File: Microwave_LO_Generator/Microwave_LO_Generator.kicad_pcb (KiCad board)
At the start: 4 copper layers, 49.5 x 47 mm, 59 parts, among them IC1 ADP150AUJZ-3.3-R7, J4 Conn_01x05_Male, U1 ADF4150HV, U2 LM317L_SO8, U3 LM317L_SO8, U4 HMC739LP4E, X1 IQXT-220-1

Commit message: update
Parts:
- added J5: Conn_01x01_Female, Microwave_LO_Generator:Connettore, F.Cu at (141.8, 99.9)
- moved C1 135.1 mm to (95.6, 95.1)
- moved C10 135.1 mm to (110.2, 102.8)
- moved C12 135.1 mm to (110.2, 104.0)
- moved C13 135.1 mm to (114.9, 103.8)
- moved C15 135.1 mm to (122.9, 103.9)
- moved C18 135.1 mm to (100.1, 109.7)
- moved C2 135.1 mm to (95.6, 93.9)
- moved C20 135.1 mm to (109.6, 118.6)
- moved C23 135.1 mm to (100.1, 84.3)
- moved C24 135.1 mm to (100.1, 86.2)
- moved C26 135.1 mm to (130.6, 102.8)
- moved C28 135.1 mm to (117.6, 98.2)
- moved C30 135.1 mm to (135.0, 94.5)
- moved C4 135.1 mm to (103.9, 97.0)
- moved C6 135.1 mm to (113.7, 94.5)
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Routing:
- net Net-(J5-Pad1): track 0.00 -> 5.42 mm
- net 0: vias 27 -> 29
- net (no net): vias 0 -> 6
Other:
- board size 49.5 x 47 mm -> 53.3 x 45.7 mm

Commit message: Power Supply update
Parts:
- removed C18, C20: 1u, Capacitor_SMD:C_0402_1005Metric_Pad0.74x0.62mm_HandSolder
- removed D3, D4, D5, D6: DIODE, Diode_SMD:D_MELF
- removed IC1: ADP150AUJZ-3.3-R7, SamacSys_Parts:SOT95P280X100-5N
- removed R10: 720r, Resistor_SMD:R_0402_1005Metric_Pad0.72x0.64mm_HandSolder
- removed R7: 0r, Resistor_SMD:R_0402_1005Metric_Pad0.72x0.64mm_HandSolder
- removed R9: 240r, Resistor_SMD:R_0402_1005Metric_Pad0.72x0.64mm_HandSolder
- added C3: 100p, Capacitor_SMD:C_0402_1005Metric_Pad0.74x0.62mm_HandSolder, F.Cu at (103.2, 109.4)
- added C31: 100p, Capacitor_SMD:C_0402_1005Metric_Pad0.74x0.62mm_HandSolder, F.Cu at (129.3, 110.7)
- added C32: 10n, Capacitor_SMD:C_0402_1005Metric_Pad0.74x0.62mm_HandSolder, F.Cu at (116.6, 84.0)
- added C33: 10n, Capacitor_SMD:C_0402_1005Metric_Pad0.74x0.62mm_HandSolder, F.Cu at (137.5, 90.3)
- added C34: 10n, Capacitor_SMD:C_0402_1005Metric_Pad0.74x0.62mm_HandSolder, F.Cu at (124.2, 107.5)
- added C35: 3.3u, Capacitor_SMD:C_0402_1005Metric_Pad0.74x0.62mm_HandSolder, F.Cu at (131.8, 94.1)
- added C36: 3.3u, Capacitor_SMD:C_0402_1005Metric_Pad0.74x0.62mm_HandSolder, F.Cu at (124.2, 104.9)
- added C5: 100p, Capacitor_SMD:C_0402_1005Metric_Pad0.74x0.62mm_HandSolder, F.Cu at (108.3, 111.9)
- added J1: Conn_01x02_Male, Connector_PinHeader_2.54mm:PinHeader_1x02_P2.54mm_Vertical, F.Cu at (102.0, 117.0)
- added J2: Conn_01x02_Male, Connector_PinHeader_2.54mm:PinHeader_1x02_P2.54mm_Vertical, F.Cu at (96.9, 86.5)
- added TP1: TestPoint, TestPoint:TestPoint_Loop_D2.60mm_Drill1.6mm_Beaded, F.Cu at (83.2, 92.5)
- added TP2: TestPoint, TestPoint:TestPoint_Loop_D2.60mm_Drill1.6mm_Beaded, F.Cu at (78.1, 92.5)
- added U5: LT1962-5, Package_SO:MSOP-8_3x3mm_P0.65mm, F.Cu at (133.1, 91.6)
- added U6: LT1962-5, Package_SO:MSOP-8_3x3mm_P0.65mm, F.Cu at (128.0, 107.5)
- C17, C19: value 1u -> 4.7u
- C21: value 1u -> 100p
- C25: value 1u -> 3.3u
- R11: value 240r -> 1K8
- R12: value 1K488 -> 300r
- R8: value 0r -> 10r
- U2: value LM317L_SO8 -> LT1962-3.3; footprint Package_SO:SOIC-8_3.9x4.9mm_P1.27mm -> Package_SO:MSOP-8_3x3mm_P0.65mm
- U3: value LM317L_SO8 -> LT3010; footprint Package_SO:SOIC-8_3.9x4.9mm_P1.27mm -> Package_SO:MSOP-8-1EP_3x3mm_P0.65mm_EP1.68x1.88mm
- moved C19 28.8 mm to (128.0, 110.6), turned to 90 degrees
- moved C24 13.5 mm to (112.8, 91.0), turned to 90 degrees
- moved C21 13.4 mm to (130.5, 87.8), turned to 180 degrees
- moved C23 13.2 mm to (111.5, 91.0), turned to 90 degrees
- moved C22 9.28 mm to (107.7, 108.7), turned to 0 degrees
- moved U3 7.02 mm to (102.6, 113.2), turned to 180 degrees
- moved U2 7.02 mm to (115.3, 87.8), turned to 270 degrees
- moved C16 6.53 mm to (102.0, 109.4), turned to 270 degrees
- moved R12 6.03 mm to (107.0, 111.9), turned to 90 degrees
- moved R11 4.74 mm to (107.7, 113.8), turned to 180 degrees
- moved D2 3.71 mm to (96.9, 116.4)
- moved C17 2.61 mm to (130.5, 89.1), turned to 180 degrees
- moved R15 2.18 mm to (133.7, 107.5)
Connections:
- C16 pad 2: +12V -> Net-(C16-Pad2)
- C17 pad 2: Net-(C17-Pad2) -> +6V
- C19 pad 2: Net-(C19-Pad2) -> +6V
- C21 pad 2: +5VA -> +6V
- C23 pad 2: +5VD -> +6V
- C24 pad 2: +5VD -> +6V
- J5 pad 2: 0 -> (no net)
- R11 pad 2: Net-(C20-Pad2) -> Net-(C5-Pad1)
- R12 pad 1: Net-(C20-Pad2) -> Net-(C5-Pad1)
- R8 pad 1: Net-(C18-Pad2) -> Net-(C16-Pad2)
- U1 pad 18: Net-(U1-Pad18) -> (no net)
- U1 pad 19: Net-(U1-Pad19) -> (no net)
- U1 pad 27: Net-(U1-Pad27) -> (no net)
- U2 pad 1: Net-(C17-Pad2) -> +3V3
- U2 pad 2: +5VA -> +3V3
- U2 pad 3: +5VA -> Net-(C32-Pad1)
- U2 pad 4: Net-(C19-Pad2) -> 0
- U2 pad 5: Net-(U2-Pad5) -> +6V
- U2 pad 6: +5VA -> (no net)
- U2 pad 7: +5VA -> (no net)
- U2 pad 8: Net-(U2-Pad8) -> +6V
- U3 pad 1: Net-(C18-Pad2) -> +9V
- U3 pad 2: +9V -> Net-(C5-Pad1)
- U3 pad 3: +9V -> (no net)
- U3 pad 4: Net-(C20-Pad2) -> 0
- U3 pad 5: Net-(U3-Pad5) -> Net-(C16-Pad2)
- U3 pad 6: +9V -> (no net)
- U3 pad 7: +9V -> (no net)
- U3 pad 8: Net-(U3-Pad8) -> Net-(C16-Pad2)
- U4 pad 1: Net-(U4-Pad1) -> (no net)
- U4 pad 12: Net-(U4-Pad12) -> (no net)
- U4 pad 13: Net-(U4-Pad13) -> (no net)
- U4 pad 14: Net-(U4-Pad14) -> (no net)
- U4 pad 18: Net-(U4-Pad18) -> (no net)
- U4 pad 19: Net-(U4-Pad19) -> (no net)
- U4 pad 21: Net-(U4-Pad21) -> (no net)
- U4 pad 23: Net-(U4-Pad23) -> (no net)
- U4 pad 24: Net-(U4-Pad24) -> (no net)
- U4 pad 3: Net-(U4-Pad3) -> (no net)
- U4 pad 5: Net-(U4-Pad5) -> (no net)
- U4 pad 6: Net-(U4-Pad6) -> (no net)
- U4 pad 7: Net-(U4-Pad7) -> (no net)
- U4 pad 8: Net-(U4-Pad8) -> (no net)
- U4 pad 9: Net-(U4-Pad9) -> (no net)
- X1 pad 1: Net-(X1-Pad1) -> (no net)
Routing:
- net +6V: track 0.00 -> 140.0 mm, vias 0 -> 2
- net +5VD: track 78.0 -> 14.7 mm, vias 2 -> 0
- net +12V: track 70.8 -> 12.6 mm, vias 2 -> 0
- net 0: track 60.1 -> 36.9 mm
- net +5VA: track 31.8 -> 12.6 mm
- net +3V3: track 73.6 -> 88.1 mm
- net Net-(C16-Pad2): track 0.00 -> 12.7 mm
- net Net-(C20-Pad2): track 11.3 -> 0.00 mm
- net Net-(C18-Pad2): track 10.5 -> 0.00 mm
- net Net-(C17-Pad2): track 10.0 -> 0.00 mm
- net Net-(C19-Pad2): track 9.46 -> 0.00 mm
- net Net-(C5-Pad1): track 0.00 -> 6.45 mm
- net +9V: track 28.7 -> 22.7 mm
- net Net-(C33-Pad1): track 0.00 -> 3.33 mm
- net Net-(C32-Pad1): track 0.00 -> 2.26 mm
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- removed copper zone on F.Cu, net +5VA
- removed copper zone on F.Cu, net +9V

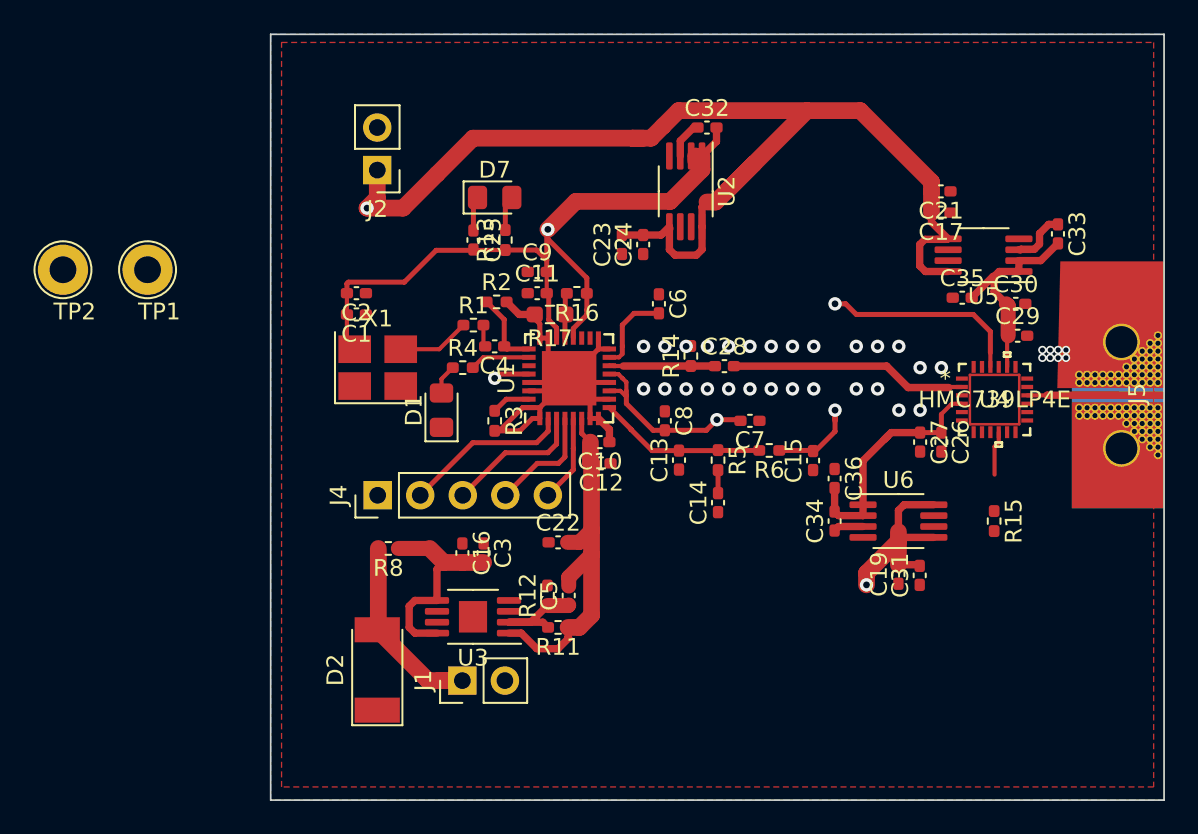
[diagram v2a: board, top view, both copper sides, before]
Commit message: Add RF/2
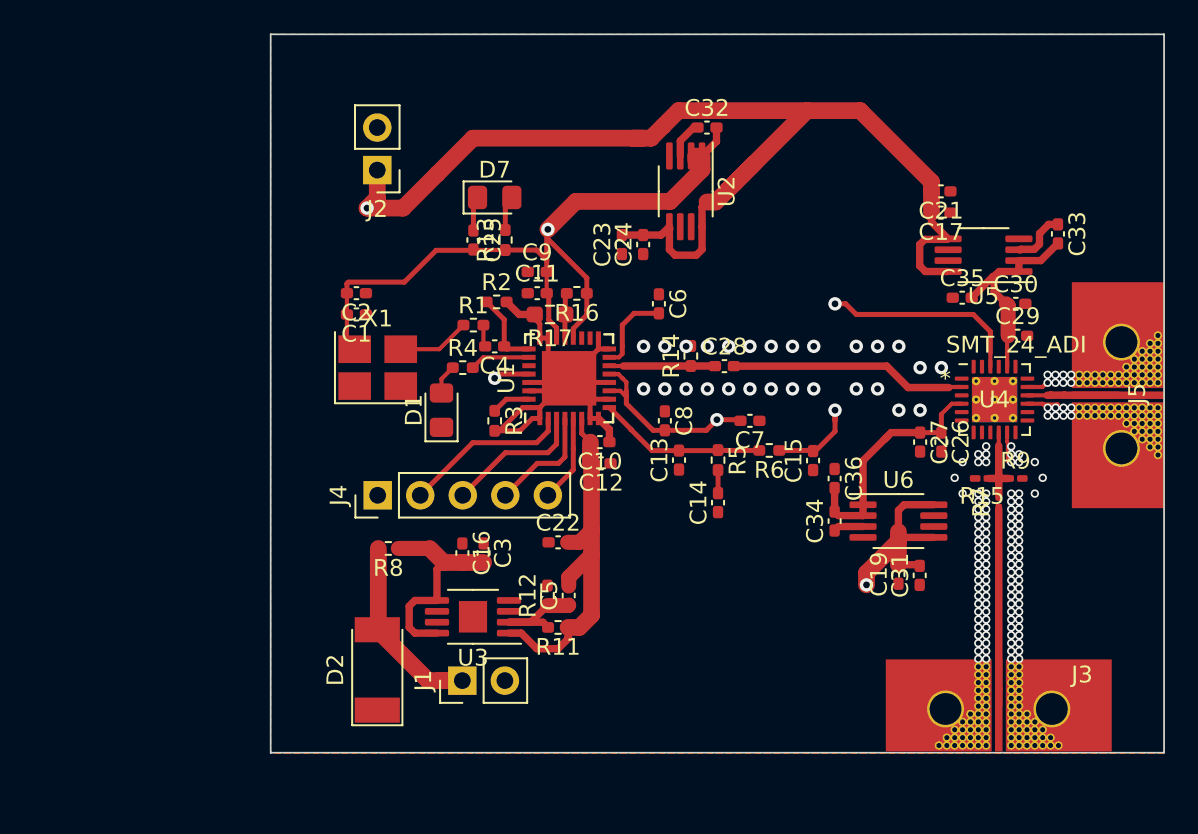
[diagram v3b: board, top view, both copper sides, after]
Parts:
- removed TP1, TP2: TestPoint, TestPoint:TestPoint_Loop_D2.60mm_Drill1.6mm_Beaded
- added J3: Conn_01x01_Female, Microwave_LO_Generator:Connettore, F.Cu at (134.1, 119.1)
- added R7: 0r, Resistor_SMD:R_0201_0603Metric_Pad0.64x0.40mm_HandSolder, F.Cu at (134.0, 106.3)
- added R9: 100r, Resistor_SMD:R_0201_0603Metric_Pad0.64x0.40mm_HandSolder, F.Cu at (135.0, 104.9)
- R15: value 51r -> 100r; footprint Resistor_SMD:R_0402_1005Metric_Pad0.72x0.64mm_HandSolder -> Resistor_SMD:R_0201_0603Metric_Pad0.64x0.40mm_HandSolder
- U4: value HMC739LP4E -> SMT_24_ADI; footprint Microwave_LO_Generator:HMC739LP4E -> Package_DFN_QFN:QFN-24-1EP_4x4mm_P0.5mm_EP2.7x2.7mm_ThermalVias
- moved R15 2.65 mm to (133.0, 104.9), turned to 180 degrees
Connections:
- J5 pad 2: (no net) -> 0
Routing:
- net Net-(J3-Pad1): track 0.00 -> 11.7 mm
- net 0: track 36.9 -> 41.8 mm, vias 29 -> 147
- net Net-(R15-Pad1): track 2.64 -> 5.09 mm
- net (no net): vias 6 -> 0
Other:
- board size 53.3 x 45.7 mm -> 53.3 x 42.9 mm
- net class GND added: clearance 0.2, trace_width 0.2, via_dia 0.8, via_drill 0.4
- rule trace_min: 0.19 -> 0.2

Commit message: A lot of change
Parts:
- added D3: DIODE, Diode_SMD:D_MELF, F.Cu at (98.6, 87.4)
- added R10: 10k, Resistor_SMD:R_0402_1005Metric_Pad0.72x0.64mm_HandSolder, F.Cu at (107.7, 108.2)
- added R18: 10k, Resistor_SMD:R_0402_1005Metric_Pad0.72x0.64mm_HandSolder, F.Cu at (104.5, 109.0)
- added R19: 10k, Resistor_SMD:R_0402_1005Metric_Pad0.72x0.64mm_HandSolder, F.Cu at (100.2, 109.0)
- added R20: 10k, Resistor_SMD:R_0402_1005Metric_Pad0.72x0.64mm_HandSolder, F.Cu at (97.9, 108.2)
- added TP1: TestPoint, TestPoint:TestPoint_Loop_D2.60mm_Drill1.6mm_Beaded, F.Cu at (100.7, 93.9)
- added TP3: TestPoint, TestPoint:TestPoint_Loop_D2.60mm_Drill1.6mm_Beaded, F.Cu at (110.2, 116.4)
- added TP4: TestPoint, TestPoint:TestPoint_Loop_D2.60mm_Drill1.6mm_Beaded, F.Cu at (134.4, 87.5)
- added TP5: TestPoint, TestPoint:TestPoint_Loop_D2.60mm_Drill1.6mm_Beaded, F.Cu at (121.6, 107.2)
- added TP6: TestPoint, TestPoint:TestPoint_Loop_D2.60mm_Drill1.6mm_Beaded, F.Cu at (109.1, 85.9)
- J3, J5: value Conn_01x01_Female -> Conn_01x02_Female
- R15, R7, R9: footprint Resistor_SMD:R_0201_0603Metric_Pad0.64x0.40mm_HandSolder -> Microwave_LO_Generator:R_0201_0603_HandSolder_mod
- U1: footprint Package_CSP:LFCSP-32-1EP_5x5mm_P0.5mm_EP3.25x3.25mm -> Microwave_LO_Generator:LFCSP-32-1EP_5x5mm_P0.5mm_mod
- U4: value SMT_24_ADI -> HMC739LP4E; footprint Package_DFN_QFN:QFN-24-1EP_4x4mm_P0.5mm_EP2.7x2.7mm_ThermalVias -> Microwave_LO_Generator:QFN-24-1EP_4x4mm_P0.5mm_EP2.7x2.7mm_ThermalVias_mod
- moved J2 5.76 mm to (102.4, 85.0), turned to 90 degrees
- moved R9 1.90 mm to (133.1, 105.0), turned to 180 degrees
- moved R15 1.90 mm to (134.9, 105.0), turned to 0 degrees
- moved R1 1.80 mm to (101.5, 97.2)
- moved R2 1.06 mm to (104.0, 95.4)
- moved C22 0.72 mm to (107.7, 109.5)
- moved R8 0.60 mm to (97.5, 109.7)
- moved R7 0.06 mm to (134.0, 106.3)
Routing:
- net +3V3: track 88.1 -> 109.1 mm, vias 3 -> 4
- net 0: track 41.8 -> 61.3 mm
- net +5VA: track 12.6 -> 19.3 mm
- net +9V: track 22.7 -> 29.0 mm
- net Net-(J4-Pad3): track 8.39 -> 12.4 mm
- net Net-(J4-Pad5): track 5.21 -> 8.85 mm
- net Net-(J3-Pad1): track 11.7 -> 14.9 mm
- net +6V: track 140.0 -> 137.0 mm
- net +5VD: track 14.7 -> 17.5 mm
- net Net-(J4-Pad4): track 6.80 -> 9.27 mm
- net Net-(J4-Pad2): track 9.98 -> 12.4 mm
- net Net-(R1-Pad1): track 4.34 -> 5.97 mm
- net Net-(C4-Pad1): track 4.78 -> 3.70 mm
- net +12V: track 12.6 -> 12.0 mm
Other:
- net class GND: trace_width 0.2 -> 0.3
- board text added: "12V GND"
- board text added: "6V GND"
- board text added: "GND CLK DATA LE CE"

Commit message: silkscreen
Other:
- board text added: "3.3V"
- board text added: "5V A"
- board text added: "5V D"
- board text added: "9V"
- board text added: "CLK"

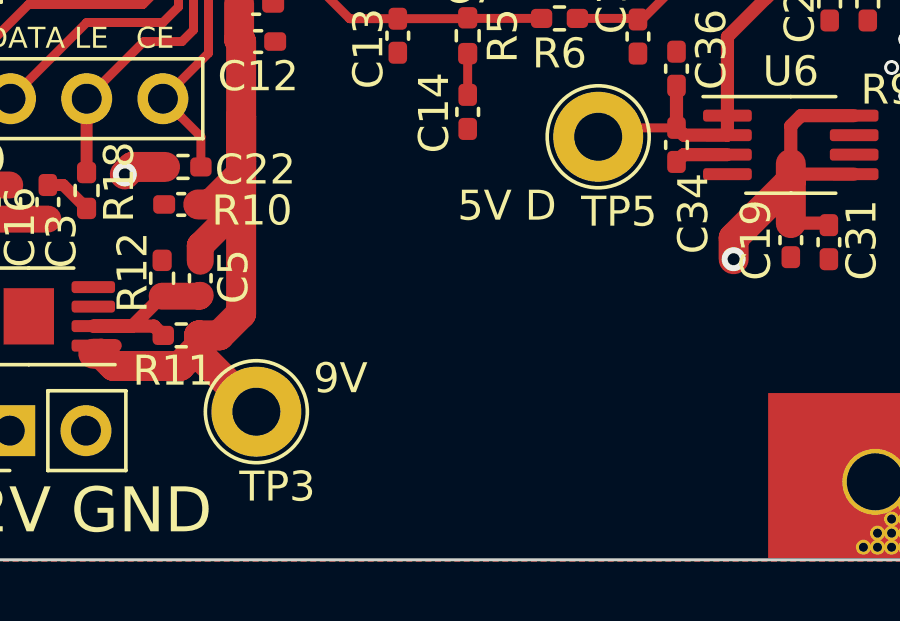
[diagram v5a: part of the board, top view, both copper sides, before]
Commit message: ADD GND test probe
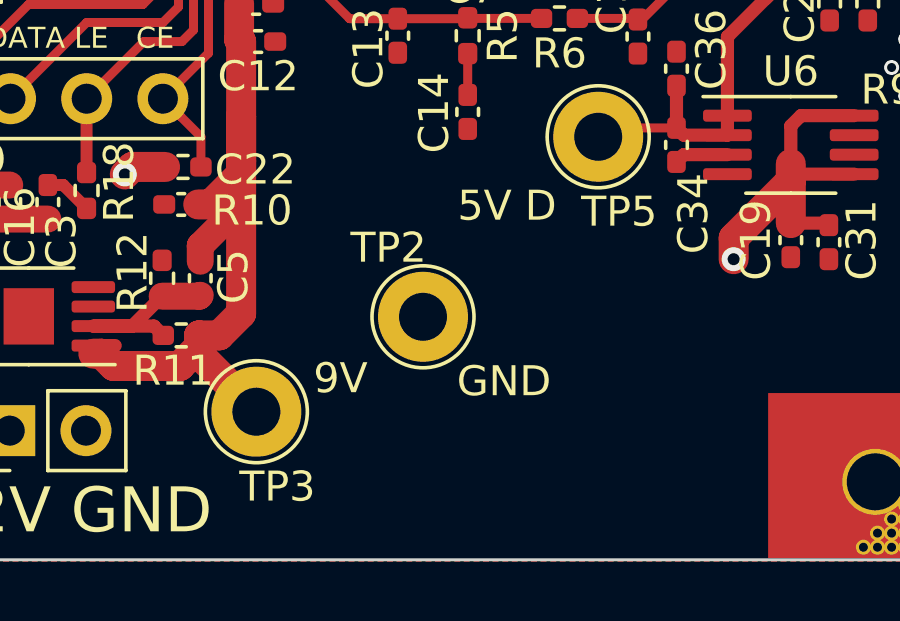
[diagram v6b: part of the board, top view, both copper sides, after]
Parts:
- added TP2: TestPoint, TestPoint:TestPoint_Loop_D2.60mm_Drill1.6mm_Beaded, F.Cu at (115.7, 113.2)
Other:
- board text added: "GND"
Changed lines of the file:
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@@
   (general
     (thickness 1.6)
-    (drawings 15)
+    (drawings 16)
     (tracks 572)
     (zones 0)
-    (modules 75)
+    (modules 76)
     (nets 34)
   )
@@
     (add_net 0)
   )
+  (module TestPoint:TestPoint_Loop_D2.60mm_Drill1.6mm_Beaded (layer F.Cu)
+    (at 115.735 113.2)
+    (descr "wire loop with bead as test point, loop diameter2.6mm, hole diameter 1.6mm")
+    (tags "test point wire loop bead")
+    (fp_text reference TP2 (at -1.15 -2.3) (layer F.SilkS)
+      (effects (font (size 1 1) (thickness 0.15)))
+    )
+    (fp_text value TestPoint (at 0 -2.8) (layer F.Fab)
+      (effects (font (size 1 1) (thickness 0.15)))
+    )
+    (fp_text user %R (at 0.7 2.5) (layer F.Fab)
+      (effects (font (size 1 1) (thickness 0.15)))
+    )
+    (fp_line (start -1.3 -0.3) (end -1.3 0.3) (layer F.Fab) (width 0.12))
+    (fp_line (start -1.3 0.3) (end 1.3 0.3) (layer F.Fab) (width 0.12))
+    (fp_line (start 1.3 0.3) (end 1.3 -0.3) (layer F.Fab) (width 0.12))
+    (fp_line (start 1.3 -0.3) (end -1.3 -0.3) (layer F.Fab) (width 0.12))
+    (fp_circle (center 0 0) (end 2 0) (layer F.CrtYd) (width 0.05))
+    (fp_circle (center 0 0) (end 1.7 0) (layer F.SilkS) (width 0.12))
+    (fp_circle (center 0 0) (end 1.5 0) (layer F.Fab) (width 0.12))
+    (pad 1 thru_hole circle (at 0 0) (size 3 3) (drill 1.6) (layers *.Cu *.Mask)
+      (net 9 0))
+    (model ${KISYS3DMOD}/TestPoint.3dshapes/TestPoint_Loop_D2.60mm_Drill1.6mm_Beaded.wrl
+      (at (xyz 0 0 0))
+      (scale (xyz 1 1 1))
+      (rotate (xyz 0 0 0))
+    )
+  )
   (module Diode_SMD:D_MELF (layer F.Cu)
     (at 98.6155 87.444 90)
@@
     )
   )
+  (gr_text GND (at 118.435 115.35) (layer F.SilkS)
+    (effects (font (size 1 1) (thickness 0.25)))
+  )
   (gr_text "5V A" (at 134.185 84.8) (layer F.SilkS)
